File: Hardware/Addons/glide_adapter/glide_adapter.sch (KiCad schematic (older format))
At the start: 6 parts, among them J1 Conn_01x05_Female, J2 Conn_01x12_Female, J3 Conn_02x05_Odd_Even

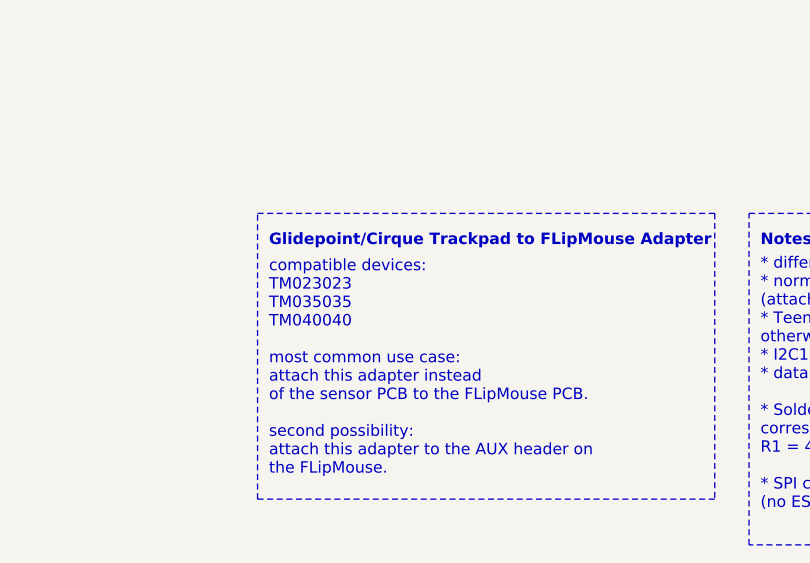
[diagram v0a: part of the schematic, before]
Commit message: Added note in README for this addon; added BOM & notes in SCH.
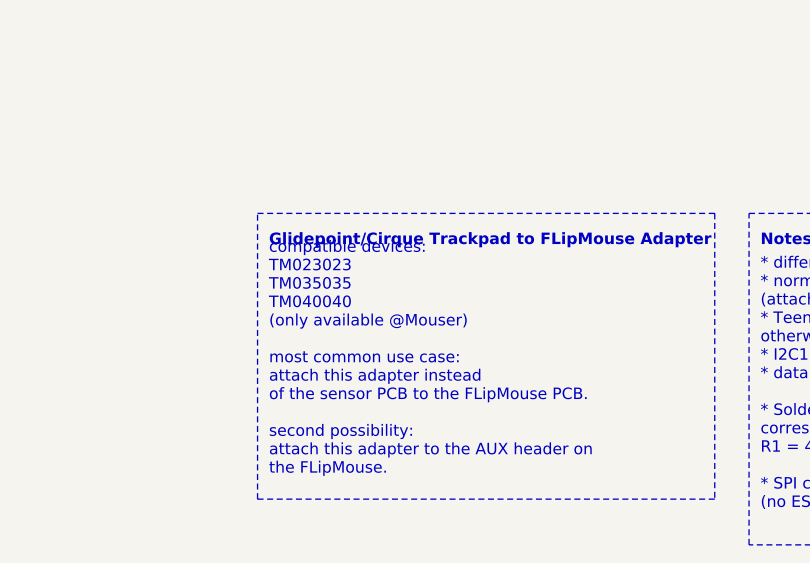
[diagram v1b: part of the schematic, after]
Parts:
- C1: Mouser (none) -> 710-885012207051
- J1: Mouser (none) -> DON'T ORDER (437-8018700510001101)
- J2: Mouser (none) -> 798-FH12-12S-0.5SH55
- J3: Mouser (none) -> DON'T ORDER
- R1: Mouser (none) -> 603-AC0805FR-7W4K7
- R2: Mouser (none) -> 603-AC0805FR-7W4K7L
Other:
- note added: "compatible devices:\nTM023023\nTM035035\nTM040040\n(only available @Mouser)\n\nmost common use case:\nattach this adapter instead\nof the sensor PCB to the FLipMouse PCB.\n\nsecond possibility:\nattach this adapter to the AUX header on \nthe FLipMouse.\n"
- note removed: "compatible devices:\nTM023023\nTM035035\nTM040040\n\nmost common use case:\nattach this adapter instead\nof the sensor PCB to the FLipMouse PCB.\n\nsecond possibility:\nattach this adapter to the AUX header on \nthe FLipMouse.\n"
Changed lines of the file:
@@
 F 2 "Connector_FFC-FPC:Hirose_FH12-12S-0.5SH_1x12-1MP_P0.50mm_Horizontal" H 2100 3150 50  0001 C CNN
 F 3 "~" H 2100 3150 50  0001 C CNN
+F 4 "798-FH12-12S-0.5SH55" H 2100 3150 50  0001 C CNN "Mouser"
 	1    2100 3150
 	1    0    0    -1
@@
 F 2 "Connector_PinSocket_2.54mm:PinSocket_1x05_P2.54mm_Vertical" H 4350 1200 50  0001 C CNN
 F 3 "~" H 4350 1200 50  0001 C CNN
+F 4 "DON'T ORDER (437-8018700510001101)" H 4350 1200 50  0001 C CNN "Mouser"
 	1    4350 1200
 	1    0    0    -1
@@
 F 2 "Resistor_SMD:R_0805_2012Metric_Pad1.20x1.40mm_HandSolder" V 1080 1300 50  0001 C CNN
 F 3 "~" H 1150 1300 50  0001 C CNN
+F 4 "603-AC0805FR-7W4K7" H 1150 1300 50  0001 C CNN "Mouser"
 	1    1150 1300
 	1    0    0    -1
@@
 F 2 "Connector_PinSocket_2.54mm:PinSocket_2x05_P2.54mm_Vertical_SMD" H 2700 1350 50  0001 C CNN
 F 3 "~" H 2700 1350 50  0001 C CNN
+F 4 "DON'T ORDER" H 2700 1350 50  0001 C CNN "Mouser"
 	1    2700 1350
 	1    0    0    -1
@@
 F 2 "Resistor_SMD:R_0805_2012Metric_Pad1.20x1.40mm_HandSolder" V 1430 1300 50  0001 C CNN
 F 3 "~" H 1500 1300 50  0001 C CNN
+F 4 "603-AC0805FR-7W4K7L" H 1500 1300 50  0001 C CNN "Mouser"
 	1    1500 1300
 	1    0    0    -1
@@
 F 2 "Capacitor_SMD:C_0805_2012Metric_Pad1.18x1.45mm_HandSolder" H 3138 3050 50  0001 C CNN
 F 3 "~" H 3100 3200 50  0001 C CNN
+F 4 "710-885012207051" H 3100 3200 50  0001 C CNN "Mouser"
 	1    3100 3200
 	1    0    0    -1
@@
 Glidepoint/Cirque Trackpad to FLipMouse Adapter
 Text Notes 6000 4050 0    50   ~ 0
-compatible devices:\nTM023023\nTM035035\nTM040040\n\nmost common use case:\nattach this adapter instead\nof the sensor PCB to the FLipMouse PCB.\n\nsecond possibility:\nattach this adapter to the AUX header on \nthe FLipMouse.\n
+compatible devices:\nTM023023\nTM035035\nTM040040\n(only available @Mouser)\n\nmost common use case:\nattach this adapter instead\nof the sensor PCB to the FLipMouse PCB.\n\nsecond possibility:\nattach this adapter to the AUX header on \nthe FLipMouse.\n
 Wire Notes Line
 	5950 2900 7950 2900

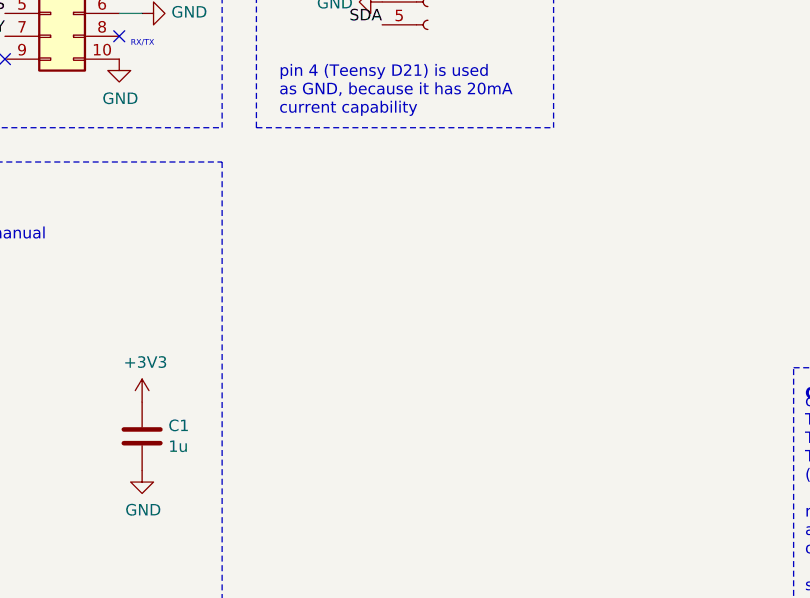
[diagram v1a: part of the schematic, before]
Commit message: Added I2C connector for SSD1306 (should be placed accordingly!); added FreeCAD design (SSD1306 is not included yet)
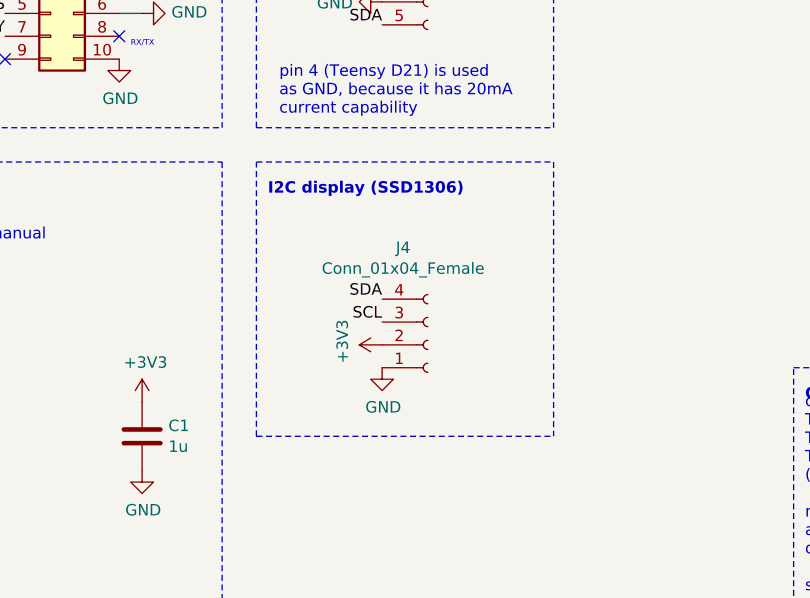
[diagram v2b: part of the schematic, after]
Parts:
- added J4: Conn_01x04_Female, Connector_PinSocket_2.54mm:PinSocket_1x04_P2.54mm_Horizontal, symbol Connector:Conn_01x04_Female
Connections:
- net +3V3: now also J4.2 (Pin_2)
- net GND: now also J4.1 (Pin_1)
- net SCL: now also J4.3 (Pin_3)
- net SDA: now also J4.4 (Pin_4)
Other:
- note added: "I2C display (SSD1306)"
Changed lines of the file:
@@
 Text Notes 8150 4200 0    50   ~ 0
 * different FM firmware is necessary\n* normally I2C is used \n(attached instead of FSR sensors)\n* Teensy D21 pin must be: OUTPUT & LOW, \notherwise no GND here.\n* I2C1 (Wire1) is used for this device\n* data ready pin is Teensy D20\n\n* Solder the resistor on the Glide pad\ncorrespondingly! (R1 missing -> I2C;\nR1 = 470k -> SPI)\n\n* SPI can be used as well, but not preferred\n(no ESP32 addon possible)
+$Comp
+L Connector:Conn_01x04_Female J4
+U 1 1 61B70E3E
+P 4350 2800
+F 0 "J4" H 4242 2375 50  0000 C CNN
+F 1 "Conn_01x04_Female" H 4242 2466 50  0000 C CNN
+F 2 "Connector_PinSocket_2.54mm:PinSocket_1x04_P2.54mm_Horizontal" H 4350 2800 50  0001 C CNN
+F 3 "~" H 4350 2800 50  0001 C CNN
+	1    4350 2800
+	1    0    0    1
+$EndComp
+$Comp
+L power:GND #PWR09
+U 1 1 61B71A08
+P 4150 2900
+F 0 "#PWR09" H 4150 2650 50  0001 C CNN
+F 1 "GND" H 4155 2727 50  0000 C CNN
+F 2 "" H 4150 2900 50  0001 C CNN
+F 3 "" H 4150 2900 50  0001 C CNN
+	1    4150 2900
+	1    0    0    -1
+$EndComp
+$Comp
+L power:+3V3 #PWR08
+U 1 1 61B71CDF
+P 4150 2800
+F 0 "#PWR08" H 4150 2650 50  0001 C CNN
+F 1 "+3V3" H 4165 2973 50  0000 C CNN
+F 2 "" H 4150 2800 50  0001 C CNN
+F 3 "" H 4150 2800 50  0001 C CNN
+	1    4150 2800
+	0    -1   -1   0
+$EndComp
+Text Label 4150 2600 2    50   ~ 0
+SDA
+Text Label 4150 2700 2    50   ~ 0
+SCL
+Text Notes 3650 2150 0    50   ~ 10
+I2C display (SSD1306)
+Wire Notes Line
+	3600 3200 3600 2000
+Wire Notes Line
+	4900 2000 4900 3200
+Wire Notes Line
+	3600 3200 4900 3200
+Wire Notes Line
+	3600 2000 4900 2000
 $EndSCHEMATC

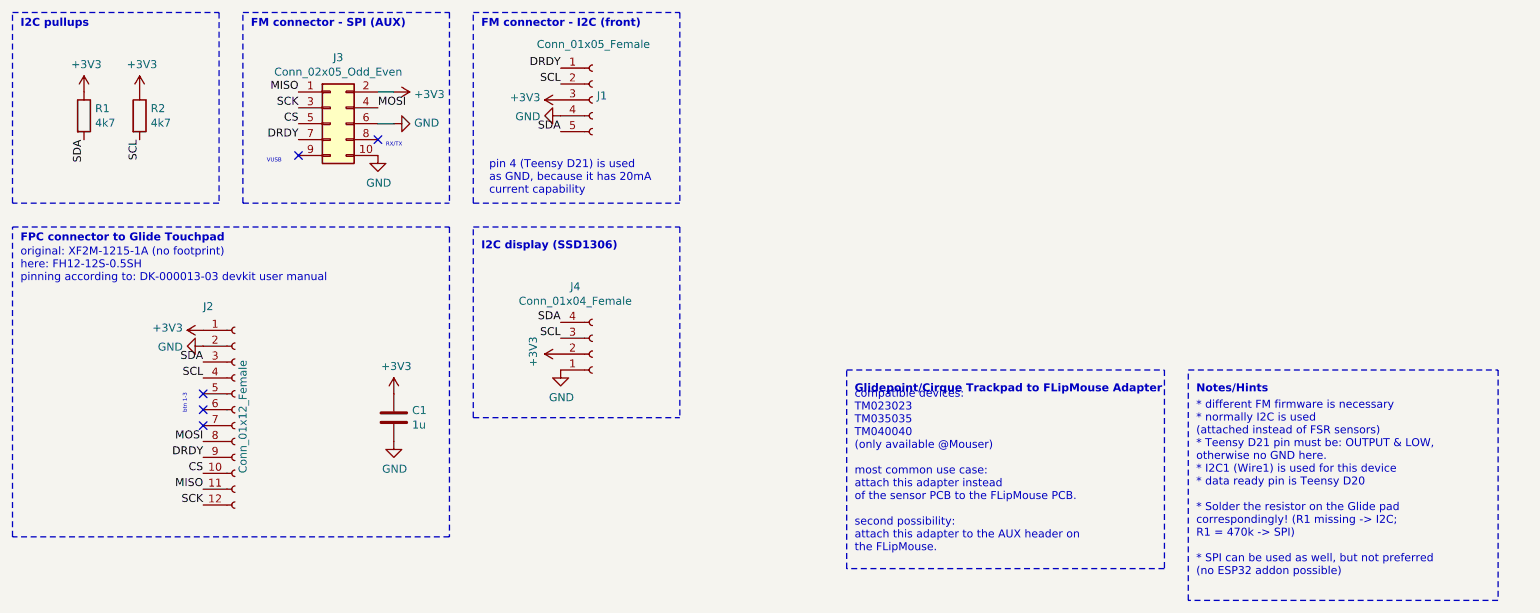
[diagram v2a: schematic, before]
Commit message: Changed case design for I2C OLED; changed PCB design (removed SPI header & added display header)
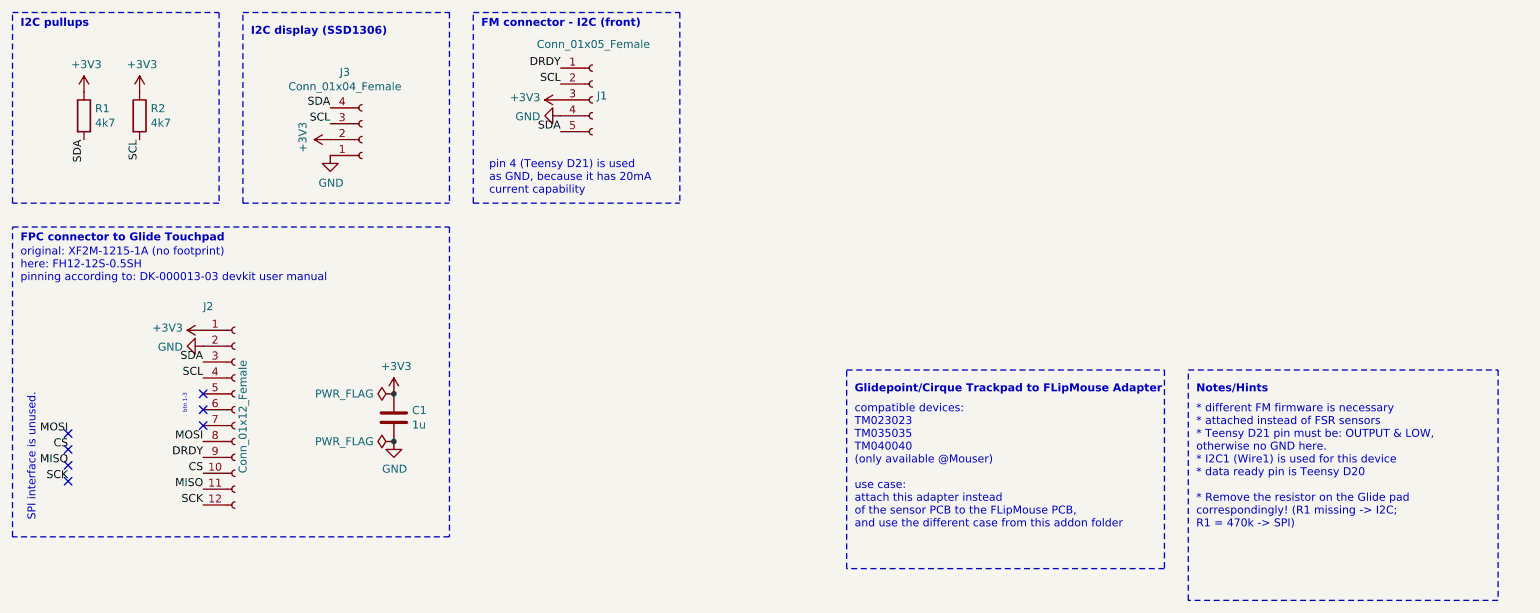
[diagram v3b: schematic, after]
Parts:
- removed J3: Conn_02x05_Odd_Even, Connector_PinSocket_2.54mm:PinSocket_2x05_P2.54mm_Vertical_SMD, symbol Connector_Generic:Conn_02x05_Odd_Even
- renumbered J4 to J3
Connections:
- no-connect marks 5 -> 7
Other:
- note added: "* different FM firmware is necessary\n* attached instead of FSR sensors\n* Teensy D21 pin must be: OUTPUT & LOW, \notherwise no GND here.\n* I2C1 (Wire1) is used for this device\n* data ready pin is Teensy D20\n\n* Remove the resistor on the Glide pad\ncorrespondingly! (R1 missing -> I2C;\nR1 = 470k -> SPI)"
- note added: "SPI interface is unused."
- note added: "compatible devices:\nTM023023\nTM035035\nTM040040\n(only available @Mouser)\n\nuse case:\nattach this adapter instead\nof the sensor PCB to the FLipMouse PCB,\nand use the different case from this addon folder"
- note removed: "* different FM firmware is necessary\n* normally I2C is used \n(attached instead of FSR sensors)\n* Teensy D21 pin must be: OUTPUT & LOW, \notherwise no GND here.\n* I2C1 (Wire1) is used for this device\n* data ready pin is Teensy D20\n\n* Solder the resistor on the Glide pad\ncorrespondingly! (R1 missing -> I2C;\nR1 = 470k -> SPI)\n\n* SPI can be used as well, but not preferred\n(no ESP32 addon 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"
- note removed: "FM connector - SPI (AUX)"
- note removed: "RX/TX"
- note removed: "VUSB"
- note removed: "compatible devices:\nTM023023\nTM035035\nTM040040\n(only available @Mouser)\n\nmost common use case:\nattach this adapter instead\nof the sensor PCB to the FLipMouse PCB.\n\nsecond possibility:\nattach this adapter to the AUX header on \nthe FLipMouse.\n"
- moved on the sheet: J3
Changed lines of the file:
@@
 SCK
-$Comp
-L Connector_Generic:Conn_02x05_Odd_Even J3
-U 1 1 61B23C89
-P 2700 1350
-F 0 "J3" H 2750 1767 50  0000 C CNN
-F 1 "Conn_02x05_Odd_Even" H 2750 1676 50  0000 C CNN
-F 2 "Connector_PinSocket_2.54mm:PinSocket_2x05_P2.54mm_Vertical_SMD" H 2700 1350 50  0001 C CNN
-F 3 "~" H 2700 1350 50  0001 C CNN
-F 4 "DON'T ORDER" H 2700 1350 50  0001 C CNN "Mouser"
-	1    2700 1350
-	1    0    0    -1
-$EndComp
 $Comp
 L Device:R R2
@@
 I2C pullups
 Wire Notes Line
-	2150 650  3450 650
-Wire Notes Line
-	2150 1850 2150 650
-Text Notes 2200 750  0    50   ~ 10
-FM connector - SPI (AUX)
-Wire Notes Line
-	2150 1850 3450 1850
-Wire Notes Line
-	3450 650  3450 1850
-Wire Notes Line
 	3600 650  4900 650
 Wire Notes Line
@@
 Text Notes 3700 1800 0    50   ~ 0
 pin 4 (Teensy D21) is used\nas GND, because it has 20mA\ncurrent capability
-NoConn ~ 2500 1550
-$Comp
-L power:GND #PWR0102
-U 1 1 61B387A6
-P 3000 1550
-F 0 "#PWR0102" H 3000 1300 50  0001 C CNN
-F 1 "GND" H 3005 1377 50  0000 C CNN
-F 2 "" H 3000 1550 50  0001 C CNN
-F 3 "" H 3000 1550 50  0001 C CNN
-	1    3000 1550
-	1    0    0    -1
-$EndComp
-$Comp
-L power:GND #PWR0103
-U 1 1 61B38B6A
-P 3100 1350
-F 0 "#PWR0103" H 3100 1100 50  0001 C CNN
-F 1 "GND" V 3105 1222 50  0000 R CNN
-F 2 "" H 3100 1350 50  0001 C CNN
-F 3 "" H 3100 1350 50  0001 C CNN
-	1    3100 1350
-	0    -1   -1   0
-$EndComp
-Wire Wire Line
-	3100 1350 3000 1350
-Text Label 2500 1150 2    50   ~ 0
-MISO
-$Comp
-L power:+3V3 #PWR0104
-U 1 1 61B393B2
-P 3100 1150
-F 0 "#PWR0104" H 3100 1000 50  0001 C CNN
-F 1 "+3V3" V 3115 1278 50  0000 L CNN
-F 2 "" H 3100 1150 50  0001 C CNN
-F 3 "" H 3100 1150 50  0001 C CNN
-	1    3100 1150
-	0    1    1    0
-$EndComp
-Text Notes 2300 1600 0    25   ~ 0
-VUSB
-NoConn ~ 3000 1450
-Text Notes 3050 1500 0    25   ~ 0
-RX/TX
-Text Label 2500 1350 2    50   ~ 0
-CS
-Text Label 2500 1250 2    50   ~ 0
-SCK
-Text Label 3000 1250 0    50   ~ 0
-MOSI
-Wire Wire Line
-	3100 1150 3000 1150
 $Comp
 L Device:C C1
@@
 	1    0    0    -1
 $EndComp
-Text Label 2500 1450 2    50   ~ 0
-DRDY
 Text Notes 6000 3050 0    50   ~ 10
 Glidepoint/Cirque Trackpad to FLipMouse Adapter
-Text Notes 6000 4050 0    50   ~ 0
-compatible devices:\nTM023023\nTM035035\nTM040040\n(only available @Mouser)\n\nmost common use case:\nattach this adapter instead\nof the sensor PCB to the FLipMouse PCB.\n\nsecond possibility:\nattach this adapter to the AUX header on \nthe FLipMouse.\n
+Text Notes 6000 3900 0    50   ~ 0
+compatible devices:\nTM023023\nTM035035\nTM040040\n(only available @Mouser)\n\nuse case:\nattach this adapter instead\nof the sensor PCB to the FLipMouse PCB,\nand use the different case from this addon folder
 Wire Notes Line
 	5950 2900 7950 2900
@@
 Wire Notes Line
 	8100 4350 8100 2900
-Text Notes 8150 4200 0    50   ~ 0
-* different FM firmware is necessary\n* normally I2C is used \n(attached instead of FSR sensors)\n* Teensy D21 pin must be: OUTPUT & LOW, \notherwise no GND here.\n* I2C1 (Wire1) is used for this device\n* data ready pin is Teensy D20\n\n* Solder the resistor on the Glide pad\ncorrespondingly! (R1 missing -> I2C;\nR1 = 470k -> SPI)\n\n* SPI can be used as well, but not preferred\n(no ESP32 addon possible)
-$Comp
-L Connector:Conn_01x04_Female J4
+Text Notes 8150 3900 0    50   ~ 0
+* different FM firmware is necessary\n* attached instead of FSR sensors\n* Teensy D21 pin must be: OUTPUT & LOW, \notherwise no GND here.\n* I2C1 (Wire1) is used for this device\n* data ready pin is Teensy D20\n\n* Remove the resistor on the Glide pad\ncorrespondingly! (R1 missing -> I2C;\nR1 = 470k -> SPI)
+$Comp
+L Connector:Conn_01x04_Female J3
 U 1 1 61B70E3E
-P 4350 2800
-F 0 "J4" H 4242 2375 50  0000 C CNN
-F 1 "Conn_01x04_Female" H 4242 2466 50  0000 C CNN
-F 2 "Connector_PinSocket_2.54mm:PinSocket_1x04_P2.54mm_Horizontal" H 4350 2800 50  0001 C CNN
-F 3 "~" H 4350 2800 50  0001 C CNN
-	1    4350 2800
+P 2900 1450
+F 0 "J3" H 2792 1025 50  0000 C CNN
+F 1 "Conn_01x04_Female" H 2792 1116 50  0000 C CNN
+F 2 "Connector_PinSocket_2.54mm:PinSocket_1x04_P2.54mm_Horizontal" H 2900 1450 50  0001 C CNN
+F 3 "~" H 2900 1450 50  0001 C CNN
+	1    2900 1450
 	1    0    0    1
 $EndComp
@@
 L power:GND #PWR09
 U 1 1 61B71A08
-P 4150 2900
-F 0 "#PWR09" H 4150 2650 50  0001 C CNN
-F 1 "GND" H 4155 2727 50  0000 C CNN
-F 2 "" H 4150 2900 50  0001 C CNN
-F 3 "" H 4150 2900 50  0001 C CNN
-	1    4150 2900
+P 2700 1550
+F 0 "#PWR09" H 2700 1300 50  0001 C CNN
+F 1 "GND" H 2705 1377 50  0000 C CNN
+F 2 "" H 2700 1550 50  0001 C CNN
+F 3 "" H 2700 1550 50  0001 C CNN
+	1    2700 1550
 	1    0    0    -1
 $EndComp
@@
 L power:+3V3 #PWR08
 U 1 1 61B71CDF
-P 4150 2800
-F 0 "#PWR08" H 4150 2650 50  0001 C CNN
-F 1 "+3V3" H 4165 2973 50  0000 C CNN
-F 2 "" H 4150 2800 50  0001 C CNN
-F 3 "" H 4150 2800 50  0001 C CNN
-	1    4150 2800
-	0    -1   -1   0
-$EndComp
-Text Label 4150 2600 2    50   ~ 0
+P 2700 1450
+F 0 "#PWR08" H 2700 1300 50  0001 C CNN
+F 1 "+3V3" H 2715 1623 50  0000 C CNN
+F 2 "" H 2700 1450 50  0001 C CNN
+F 3 "" H 2700 1450 50  0001 C CNN
+	1    2700 1450
+	0    -1   -1   0
+$EndComp
+Text Label 2700 1250 2    50   ~ 0
 SDA
-Text Label 4150 2700 2    50   ~ 0
+Text Label 2700 1350 2    50   ~ 0
 SCL
-Text Notes 3650 2150 0    50   ~ 10
+Text Notes 2200 800  0    50   ~ 10
 I2C display (SSD1306)
 Wire Notes Line
-	3600 3200 3600 2000
-Wire Notes Line
-	4900 2000 4900 3200
-Wire Notes Line
-	3600 3200 4900 3200
-Wire Notes Line
-	3600 2000 4900 2000
+	2150 1850 2150 650
+Wire Notes Line
+	3450 650  3450 1850
+Wire Notes Line
+	2150 1850 3450 1850
+Wire Notes Line
+	2150 650  3450 650
+Text Label 1050 3300 2    50   ~ 0
+MOSI
+Text Label 1050 3400 2    50   ~ 0
+CS
+Text Label 1050 3500 2    50   ~ 0
+MISO
+Text Label 1050 3600 2    50   ~ 0
+SCK
+NoConn ~ 1050 3600
+NoConn ~ 1050 3500
+NoConn ~ 1050 3400
+NoConn ~ 1050 3300
+Text Notes 850  3850 1    50   ~ 0
+SPI interface is unused.
+$Comp
+L power:PWR_FLAG #FLG0101
+U 1 1 61B90D39
+P 3100 3050
+F 0 "#FLG0101" H 3100 3125 50  0001 C CNN
+F 1 "PWR_FLAG" V 3100 3177 50  0000 L CNN
+F 2 "" H 3100 3050 50  0001 C CNN
+F 3 "~" H 3100 3050 50  0001 C CNN
+	1    3100 3050
+	0    -1   -1   0
+$EndComp
+Connection ~ 3100 3050
+$Comp
+L power:PWR_FLAG #FLG0102
+U 1 1 61B91308
+P 3100 3350
+F 0 "#FLG0102" H 3100 3425 50  0001 C CNN
+F 1 "PWR_FLAG" V 3100 3477 50  0000 L CNN
+F 2 "" H 3100 3350 50  0001 C CNN
+F 3 "~" H 3100 3350 50  0001 C CNN
+	1    3100 3350
+	0    -1   -1   0
+$EndComp
+Connection ~ 3100 3350
 $EndSCHEMATC

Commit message: Updated SCH/BOM with correct product number for pinhdr
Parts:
- J3: footprint Connector_PinSocket_2.54mm:PinSocket_1x04_P2.54mm_Horizontal -> Connector_Harwin:Harwin_M20-89004xx_1x04_P2.54mm_Horizontal; Mouser (none) -> 801-87-004-40-002101
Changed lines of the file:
@@
 F 0 "J3" H 2792 1025 50  0000 C CNN
 F 1 "Conn_01x04_Female" H 2792 1116 50  0000 C CNN
-F 2 "Connector_PinSocket_2.54mm:PinSocket_1x04_P2.54mm_Horizontal" H 2900 1450 50  0001 C CNN
+F 2 "Connector_Harwin:Harwin_M20-89004xx_1x04_P2.54mm_Horizontal" H 2900 1450 50  0001 C CNN
 F 3 "~" H 2900 1450 50  0001 C CNN
+F 4 "801-87-004-40-002101" H 2900 1450 50  0001 C CNN "Mouser"
 	1    2900 1450
 	1    0    0    1
